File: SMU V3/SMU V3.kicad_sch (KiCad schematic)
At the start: 3 parts

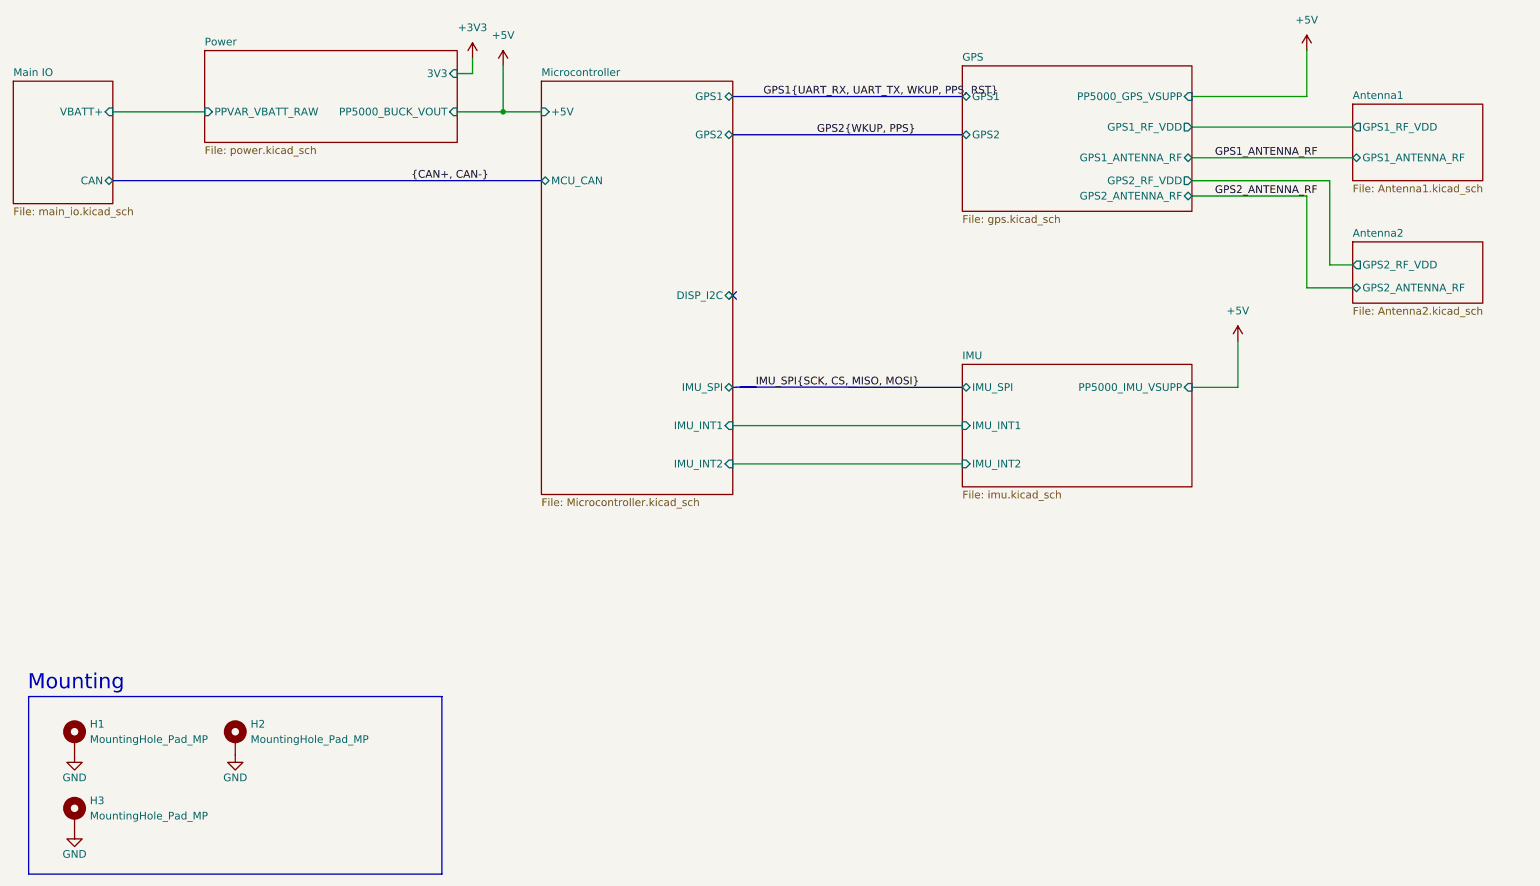
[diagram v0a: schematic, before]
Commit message: improved V3
added uart/spi test points and status leds
removed main 3v3 ldo
added silkscreen
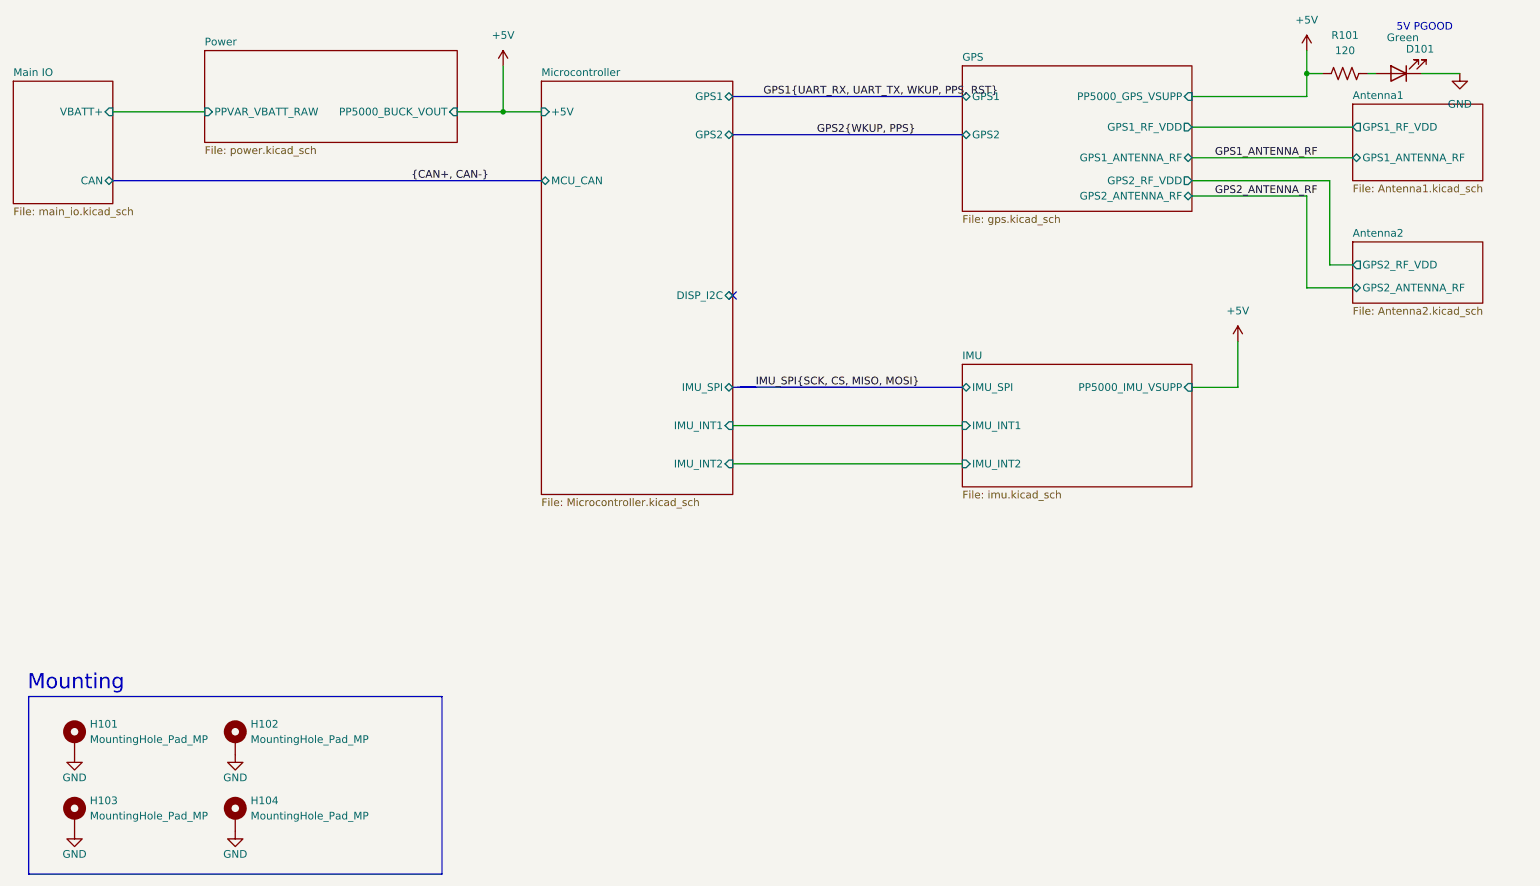
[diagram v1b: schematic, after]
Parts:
- added D101: Green, Diode_SMD:D_0805_2012Metric_Pad1.15x1.40mm_HandSolder, symbol bfr_diodes:KT-0805G
- added H104: MountingHole_Pad_MP, MountingHole:MountingHole_2.7mm_M2.5_Pad_Via, symbol Mechanical:MountingHole_Pad
- added R101: 120, Resistor_SMD:R_0603_1608Metric_Pad0.98x0.95mm_HandSolder, symbol bfr_resistors:RMCF0603FT120R
- renumbered H1 to H101, H2 to H102, H3 to H103
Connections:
- net +5V: now also R101.1
- net GND: now also D101.1 (K), H104.1
- new net: D101.2 (A), R101.2
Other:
- sheet Power ports: added none; removed 3V3
- note added: "5V PGOOD"

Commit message: actual final v3
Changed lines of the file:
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@@
 	)
 	(label "GPS1{UART_RX, UART_TX, WKUP, PPS, RST}"
-		(at 149.86 62.23 0)
+		(at 146.05 62.23 0)
 		(effects
 			(font
@@
 			(width 0.1524)
 			(type solid)
+			(color 72 0 0 1)
 		)
 		(fill
